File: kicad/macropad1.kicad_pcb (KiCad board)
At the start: 2 copper layers, 139.7 x 69.8 mm, 73 parts, among them J1 Conn_01x04, J2 USB_B_Mini, J3 AVR-ISP-6, P1 TestPoint, P20 TestPoint, P21 TestPoint, P28 TestPoint, P29 TestPoint, P30 TestPoint, P31 TestPoint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

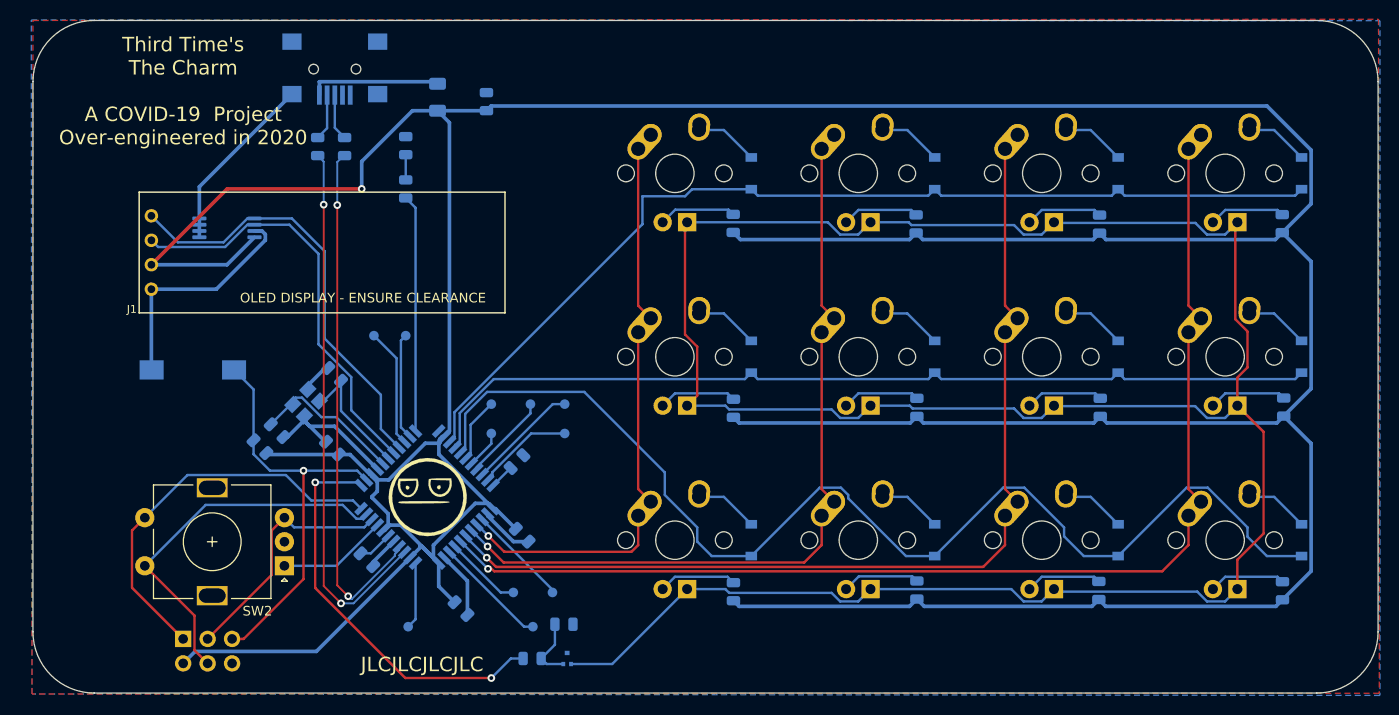
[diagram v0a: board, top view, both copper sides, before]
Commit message: Adds iBom and final revision of board
Puts holes in the right place for the case
Adds proper backlight support with a properly sized mosfet (tiny)
Double checks dimensions
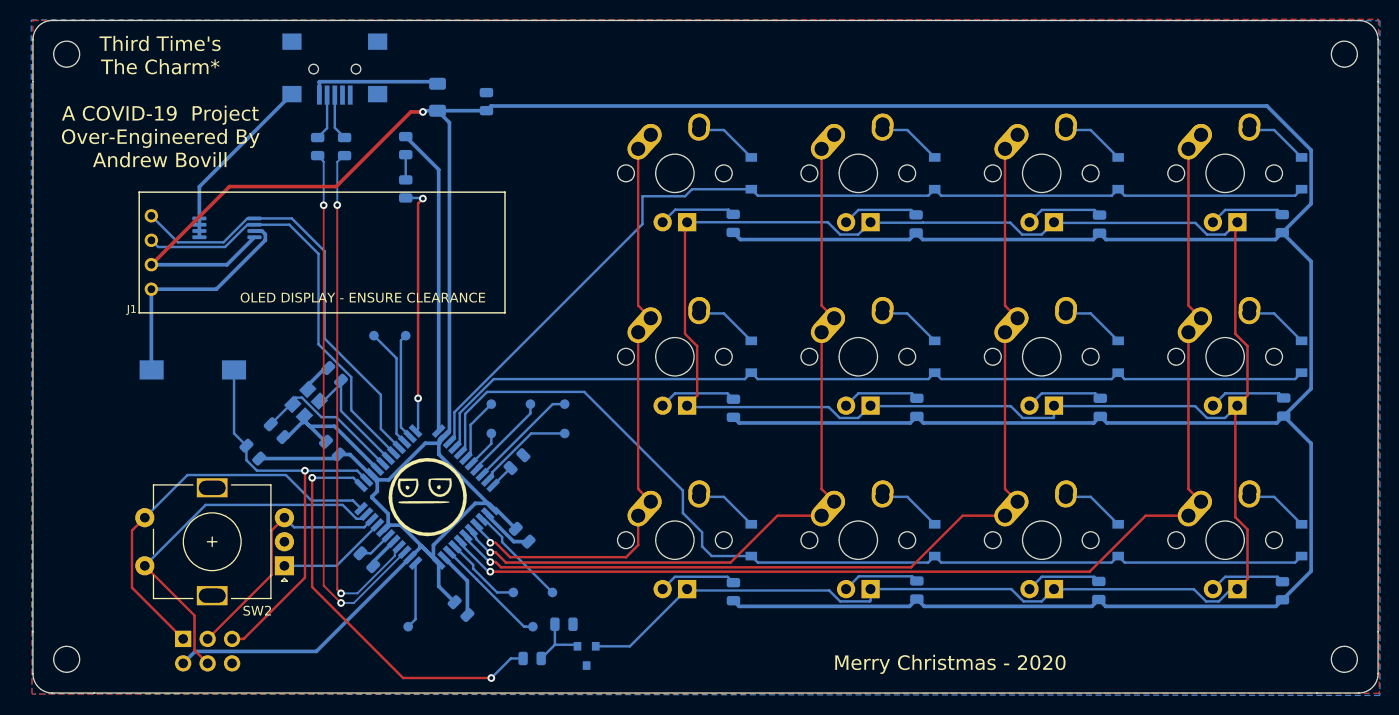
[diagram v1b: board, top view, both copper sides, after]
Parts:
- added H1: MountingHole, MountingHole:MountingHole_2.7mm_M2.5, F.Cu at (37.2, 86.7)
- added H2: MountingHole, MountingHole:MountingHole_2.7mm_M2.5, F.Cu at (169.9, 86.7)
- added H3: MountingHole, MountingHole:MountingHole_2.7mm_M2.5, F.Cu at (169.9, 23.9)
- added H4: MountingHole, MountingHole:MountingHole_2.7mm_M2.5, F.Cu at (37.2, 23.9)
- Q1: value Q_NMOS_DGS -> Q_NMOS_GDS; footprint Package_TO_SOT_SMD:SOT-723 -> Package_TO_SOT_SMD:SOT-23
- R6: value 470 -> 20k
- moved Q1 2.04 mm to (91.2, 86.3), turned to 270 degrees
- moved R4 0.93 mm to (56.5, 65.2)
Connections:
- Q1 pad 1: Net-(MX1-Pad4) -> Net-(Q1-Pad1)
- Q1 pad 2: Net-(Q1-Pad2) -> Net-(MX1-Pad4)
- R6 pad 1: Net-(Q1-Pad2) -> Net-(Q1-Pad1)
- R7 pad 1: Net-(Q1-Pad2) -> Net-(Q1-Pad1)
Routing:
- net GND: track 77.6 -> 109.6 mm
- net /ROW_2: track 120.3 -> 103.0 mm
- net Net-(Q1-Pad2): track 6.68 -> 0.00 mm
- net Net-(Q1-Pad1): track 0.00 -> 6.56 mm
- net Net-(MX1-Pad4): track 257.8 -> 254.7 mm
- net /COL_3: track 117.4 -> 115.7 mm
- net /COL_2: track 97.6 -> 96.0 mm
- net /status_led: track 24.6 -> 26.3 mm, vias 0 -> 2
- net /COL_1: track 77.8 -> 76.3 mm
- net /PWM1: track 42.2 -> 43.4 mm
- net /!RESET: track 43.7 -> 44.6 mm
- net +5V: track 503.8 -> 502.9 mm
- net /COL_0: track 57.5 -> 58.2 mm
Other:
- outline, holes or cut-outs redrawn
- board text added: "* But this was the 4th..."
- board text added: "Merry Christmas - 2020"
- board text added: "Third Time's The Charm* A COVID-19 Project Over-Engineered By Andrew Bovill"
- board text removed: "Third Time's The Charm A COVID-19 Project Over-engineered in 2020"
